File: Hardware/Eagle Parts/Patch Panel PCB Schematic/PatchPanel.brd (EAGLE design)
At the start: 226 x 102.5 mm, 25 parts

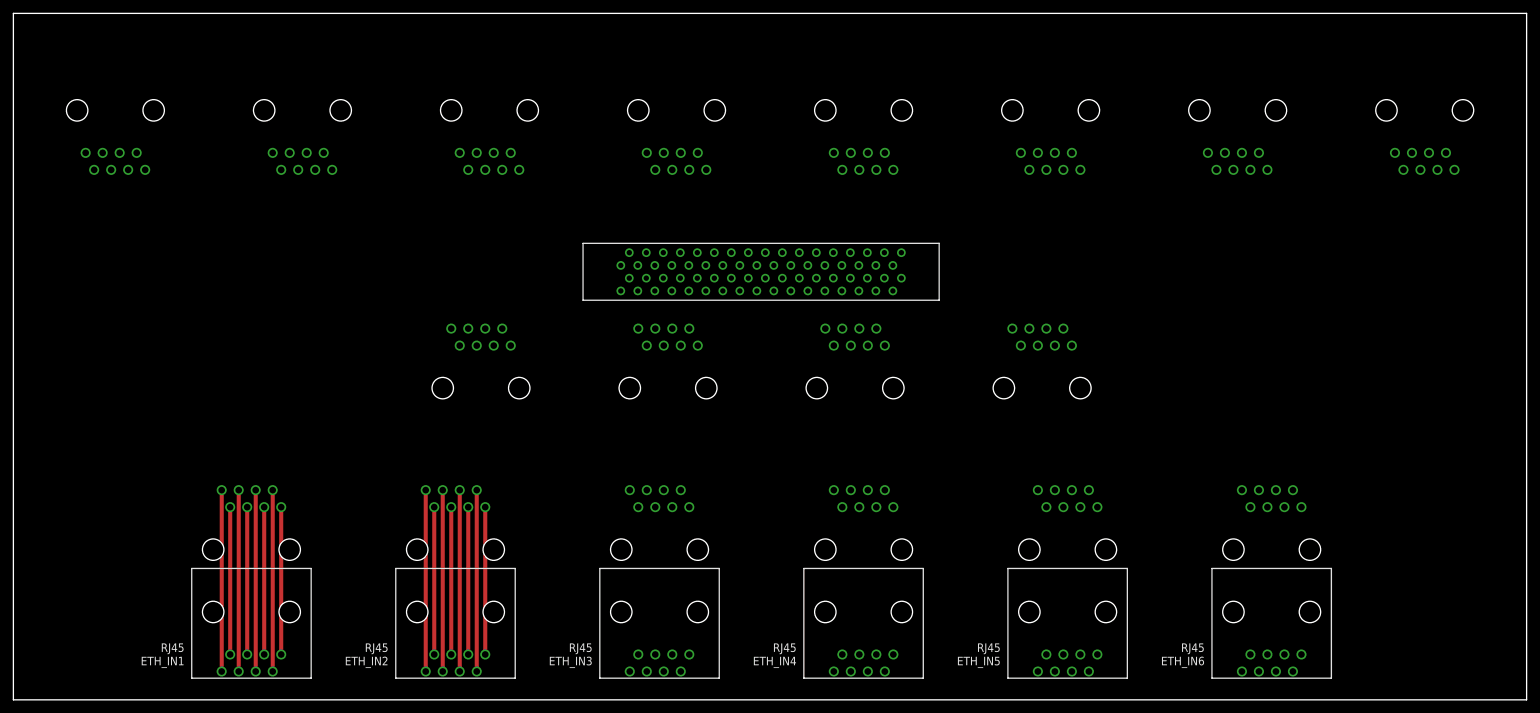
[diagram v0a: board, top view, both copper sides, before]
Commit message: Added power connections to patch panel
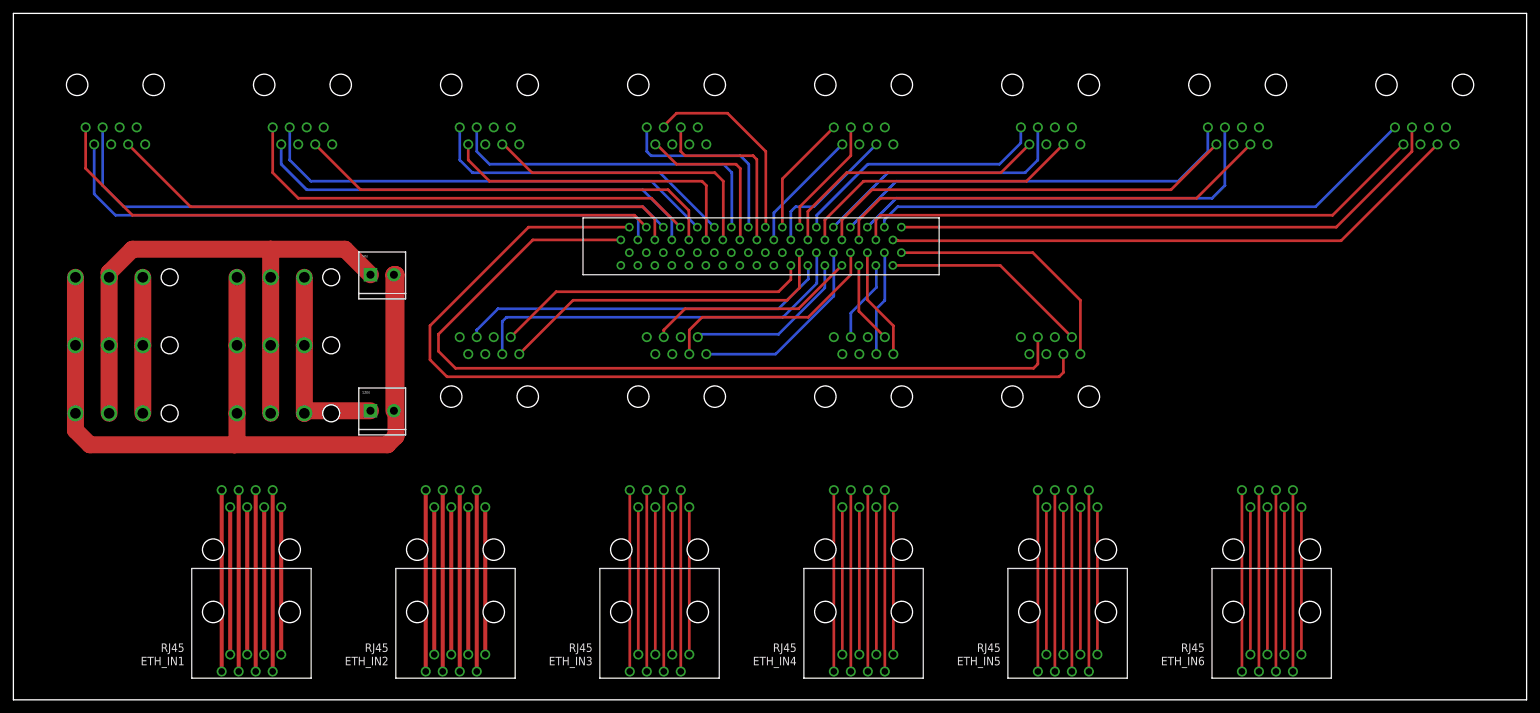
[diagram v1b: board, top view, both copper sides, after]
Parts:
- added 12IN, 5IN: M023.5MM, SparkFun-Connectors:SCREWTERMINAL-3.5MM-2
- added U$2, U$3, U$4, U$5, U$6, U$7: 3PIN, molex-power:0.93"
- moved RS-485_OUT1 3.81 mm to (210.8, 90.2)
- moved RS-485_OUT2 3.81 mm to (182.9, 90.2)
- moved RS-485_OUT3 3.81 mm to (154.9, 90.2)
- moved RS-485_OUT4 3.81 mm to (127.0, 90.2)
- moved RS-485_OUT5 3.81 mm to (99.1, 90.2)
- moved RS-485_OUT6 3.81 mm to (71.1, 90.2)
- moved RS-485_OUT7 3.81 mm to (43.2, 90.2)
- moved RS-485_OUT8 3.81 mm to (15.2, 90.2)
- moved U$1 3.81 mm to (85.1, 63.5)
- moved RS-485_OUT12 1.80 mm to (71.1, 47.0)
- moved RS-485_OUT9 1.80 mm to (154.9, 47.0)
- moved RS-485_OUT10 1.80 mm to (127.0, 47.0)
- moved RS-485_OUT11 1.80 mm to (99.1, 47.0)
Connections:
- new net +12V: 12IN.1, U$2.1, U$3.1, U$4.1, U$5.1, U$6.1, U$7.1
- new net +5V: 5IN.1, U$2.2, U$3.2, U$4.2, U$5.2, U$6.2, U$7.2
- new net GND: 12IN.2, 5IN.2, U$2.3, U$3.3, U$4.3, U$5.3, U$6.3, U$7.3
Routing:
- net GND: track 0.00 -> 142.1 mm
- net 9_TX+: track 0.00 -> 139.6 mm
- net 9_TX-: track 0.00 -> 130.5 mm
- net 8_TX+: track 0.00 -> 95.0 mm
- net 8_RX+: track 0.00 -> 93.5 mm
- net 8_RX-: track 0.00 -> 93.3 mm
- net +5V: track 0.00 -> 87.6 mm
- net 1_TX-: track 0.00 -> 87.4 mm
- net 1_RX-: track 0.00 -> 86.5 mm
- net 8_TX-: track 0.00 -> 86.4 mm
- net 1_TX+: track 0.00 -> 84.6 mm
- net 1_RX+: track 0.00 -> 83.1 mm
- net 7_RX+: track 0.00 -> 71.0 mm
- net 7_TX+: track 0.00 -> 69.9 mm
- net 7_RX-: track 0.00 -> 67.8 mm
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
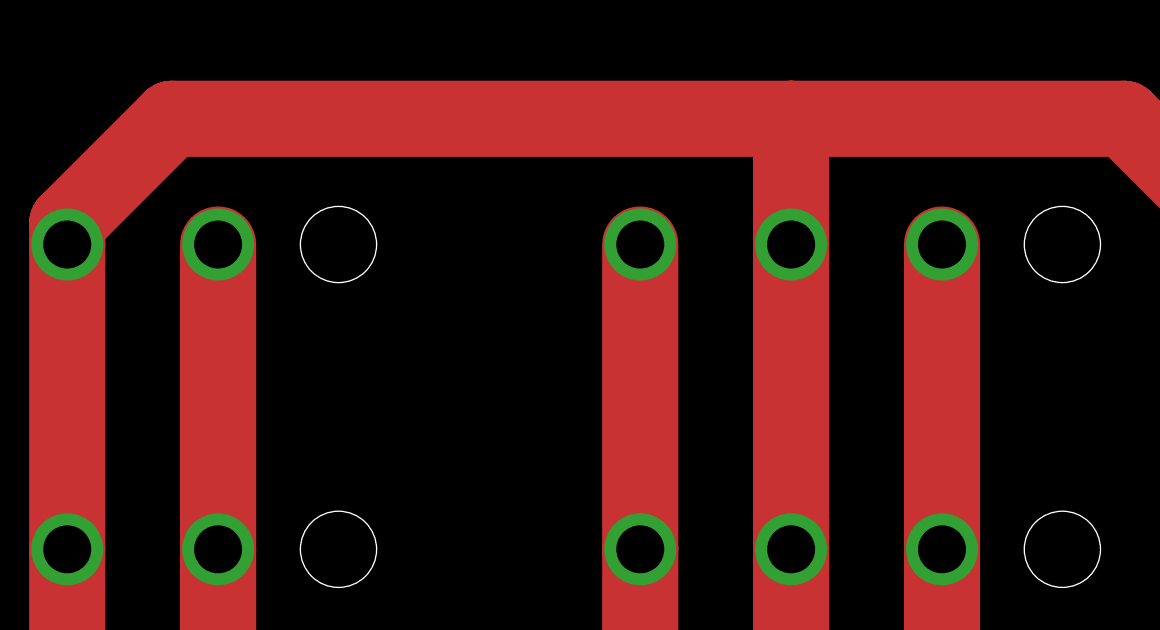
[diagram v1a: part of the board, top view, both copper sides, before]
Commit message: Fixed missing trace on patch panel board
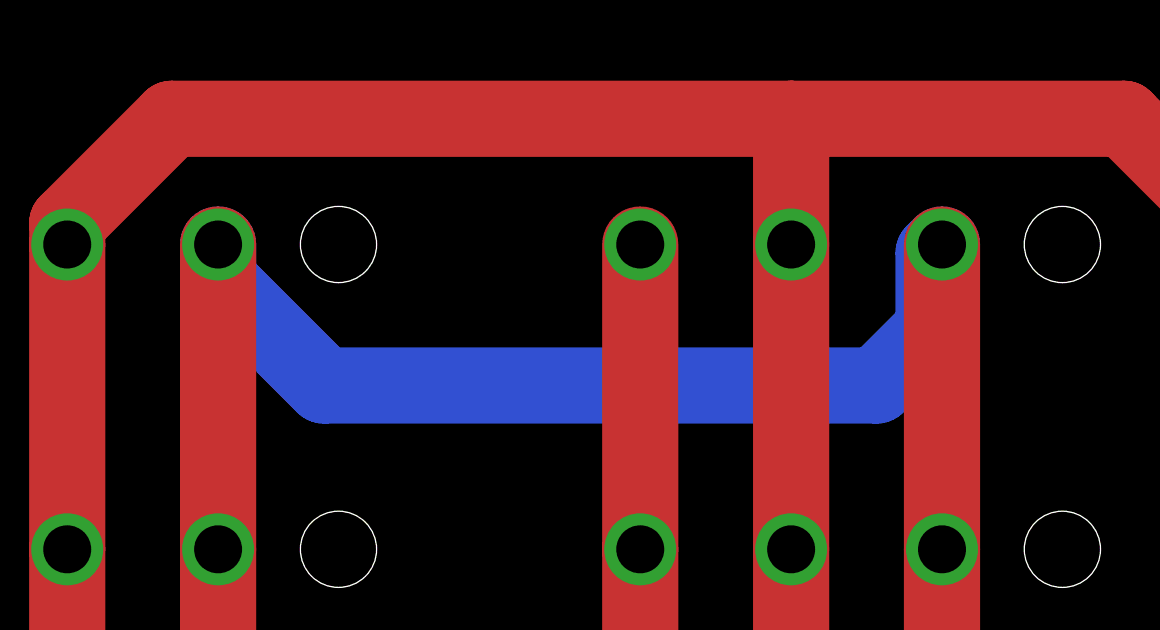
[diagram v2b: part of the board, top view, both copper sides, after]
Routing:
- net +12V: track 50.7 -> 80.9 mm
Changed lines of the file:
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@@
 <wire x1="43.4594" y1="42.799" x2="43.8404" y2="43.18" width="2.54" layer="1"/>
 <wire x1="43.8404" y1="43.18" x2="53.34" y2="43.18" width="2.54" layer="1"/>
-<wire x1="19.3294" y1="63.119" x2="43.4594" y2="63.119" width="0" layer="19" extent="1-1"/>
+<wire x1="43.4594" y1="63.119" x2="43.18" y2="62.8396" width="2.54" layer="16"/>
+<wire x1="43.18" y1="62.8396" x2="43.18" y2="60.325" width="2.54" layer="16"/>
+<wire x1="43.18" y1="60.325" x2="41.275" y2="58.42" width="2.54" layer="16"/>
+<wire x1="41.275" y1="58.42" x2="22.86" y2="58.42" width="2.54" layer="16"/>
+<wire x1="22.86" y1="58.42" x2="19.3294" y2="61.9506" width="2.54" layer="16"/>
+<wire x1="19.3294" y1="61.9506" x2="19.3294" y2="63.119" width="2.54" layer="16"/>
 </signal>
 <signal name="+5V">
